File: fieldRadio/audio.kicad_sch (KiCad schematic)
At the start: 41 parts, among them J10 Conn_01x03, U6 LM386

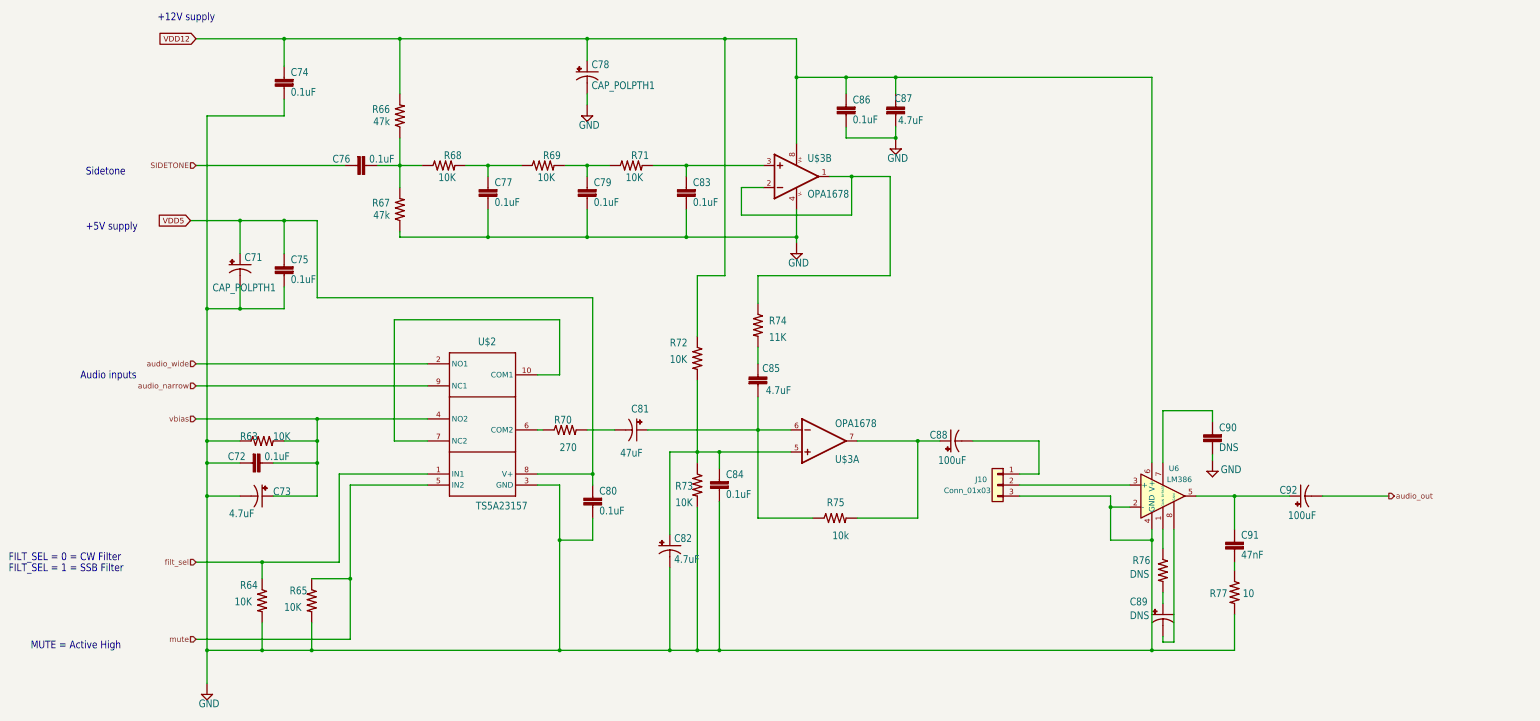
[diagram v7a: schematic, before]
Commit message: Refine Placement 2
Finish refining block placement; ready for initial routing work.
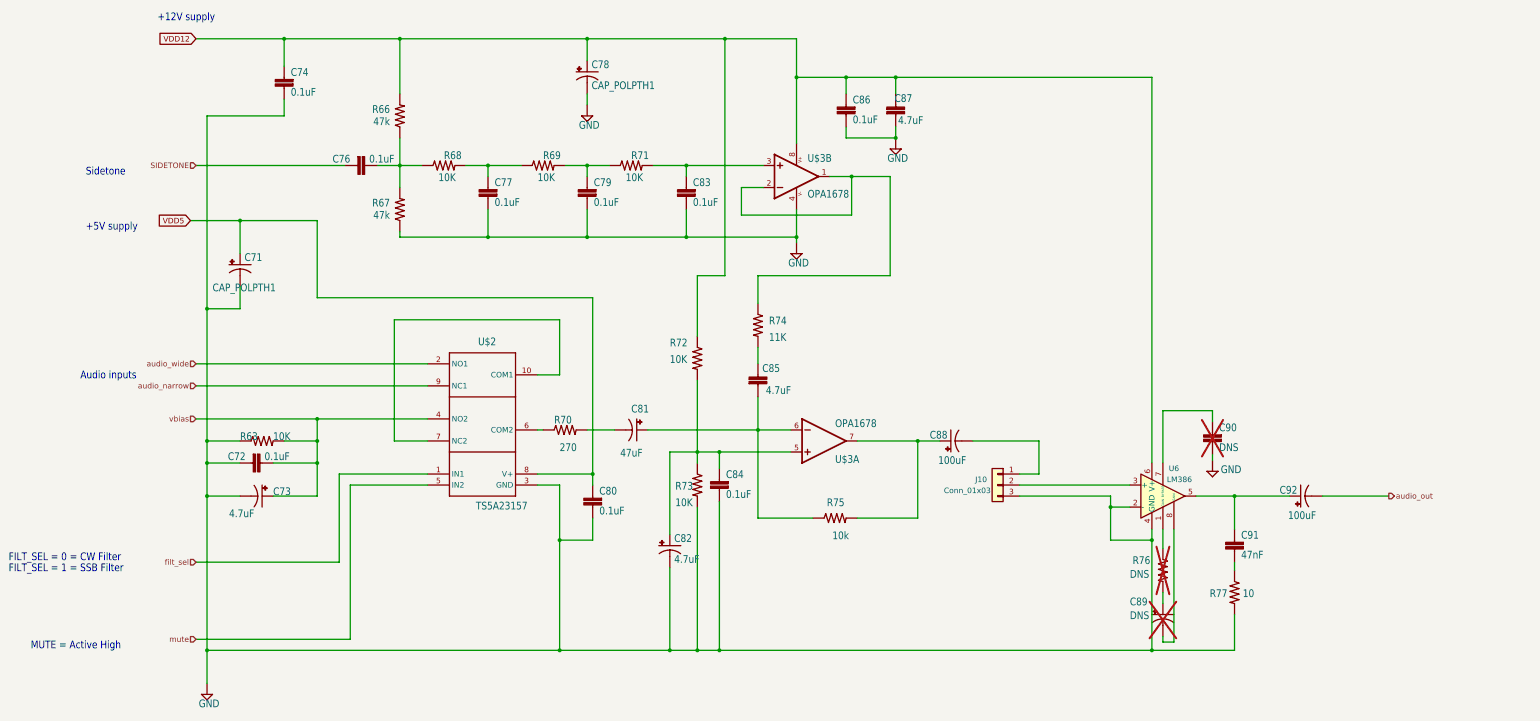
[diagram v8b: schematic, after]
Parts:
- removed C75: 0.1uF, Capacitor_SMD:C_0603_1608Metric_Pad1.08x0.95mm_HandSolder, symbol audioModule2-eagle-import:CAP0603-CAP
- removed R64, R65: 10K, Resistor_SMD:R_0603_1608Metric_Pad0.98x0.95mm_HandSolder, symbol audioModule2-eagle-import:RESISTOR0603-RES
- C89, C90, R76: now not fitted
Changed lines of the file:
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@@
   (junction (at 172.72 137.16) (diameter 0) (color 0 0 0 0)
   )
-  (junction (at 101.6 78.74) (diameter 0) (color 0 0 0 0)
-  )
   (junction (at 231.14 45.72) (diameter 0) (color 0 0 0 0)
   )
   (junction (at 109.22 124.46) (diameter 0) (color 0 0 0 0)
   )
-  (junction (at 116.84 161.29) (diameter 0) (color 0 0 0 0)
-  )
   (junction (at 196.85 177.8) (diameter 0) (color 0 0 0 0)
   )
@@
   (junction (at 109.22 129.54) (diameter 0) (color 0 0 0 0)
   )
-  (junction (at 91.44 99.06) (diameter 0) (color 0 0 0 0)
-  )
   (junction (at 194.31 66.04) (diameter 0) (color 0 0 0 0)
   )
   (junction (at 165.1 152.4) (diameter 0) (color 0 0 0 0)
   )
-  (junction (at 107.95 177.8) (diameter 0) (color 0 0 0 0)
-  )
   (junction (at 101.6 36.83) (diameter 0) (color 0 0 0 0)
   )
@@
   (junction (at 196.85 132.08) (diameter 0) (color 0 0 0 0)
   )
-  (junction (at 96.52 157.48) (diameter 0) (color 0 0 0 0)
-  )
   (junction (at 148.59 82.55) (diameter 0) (color 0 0 0 0)
   )
   (junction (at 201.93 177.8) (diameter 0) (color 0 0 0 0)
   )
-  (junction (at 96.52 177.8) (diameter 0) (color 0 0 0 0)
-  )
   (junction (at 128.27 36.83) (diameter 0) (color 0 0 0 0)
   )
   (junction (at 83.82 99.06) (diameter 0) (color 0 0 0 0)
   )
-  (wire (pts (xy 101.6 93.98) (xy 101.6 99.06))
-    (stroke (width 0) (type default))
-  )
   (wire (pts (xy 275.59 129.54) (xy 275.59 137.16))
     (stroke (width 0) (type default))
@@
     (stroke (width 0) (type default))
   )
-  (wire (pts (xy 81.28 157.48) (xy 96.52 157.48))
+  (wire (pts (xy 81.28 157.48) (xy 114.3 157.48))
     (stroke (width 0) (type default))
   )
@@
     (stroke (width 0) (type default))
   )
-  (wire (pts (xy 96.52 171.45) (xy 96.52 177.8))
-    (stroke (width 0) (type default))
-  )
-  (wire (pts (xy 116.84 161.29) (xy 116.84 139.7))
+  (wire (pts (xy 116.84 139.7) (xy 116.84 175.26))
     (stroke (width 0) (type default))
   )
@@
     (stroke (width 0) (type default))
   )
-  (wire (pts (xy 101.6 99.06) (xy 91.44 99.06))
-    (stroke (width 0) (type default))
-  )
   (wire (pts (xy 231.14 57.15) (xy 231.14 59.69))
     (stroke (width 0) (type default))
@@
     (stroke (width 0) (type default))
   )
-  (wire (pts (xy 101.6 78.74) (xy 109.22 78.74))
-    (stroke (width 0) (type default))
-  )
   (wire (pts (xy 301.625 152.4) (xy 301.625 177.8))
     (stroke (width 0) (type default))
@@
     (stroke (width 0) (type default))
   )
-  (wire (pts (xy 91.44 78.74) (xy 101.6 78.74))
+  (wire (pts (xy 91.44 78.74) (xy 109.22 78.74))
     (stroke (width 0) (type default))
   )
@@
     (stroke (width 0) (type default))
   )
-  (wire (pts (xy 96.52 157.48) (xy 96.52 161.29))
-    (stroke (width 0) (type default))
-  )
   (wire (pts (xy 128.27 59.69) (xy 128.27 66.04))
     (stroke (width 0) (type default))
@@
     (stroke (width 0) (type default))
   )
-  (wire (pts (xy 116.84 175.26) (xy 116.84 161.29))
-    (stroke (width 0) (type default))
-  )
   (wire (pts (xy 304.165 174.625) (xy 304.165 175.895))
     (stroke (width 0) (type default))
   )
-  (wire (pts (xy 101.6 86.36) (xy 101.6 78.74))
-    (stroke (width 0) (type default))
-  )
   (wire (pts (xy 160.02 114.3) (xy 165.1 114.3))
     (stroke (width 0) (type default))
@@
     (stroke (width 0) (type default))
   )
-  (wire (pts (xy 107.95 171.45) (xy 107.95 177.8))
-    (stroke (width 0) (type default))
-  )
   (wire (pts (xy 99.06 134.62) (xy 109.22 134.62))
     (stroke (width 0) (type default))
@@
     (stroke (width 0) (type default))
   )
-  (wire (pts (xy 107.95 161.29) (xy 116.84 161.29))
-    (stroke (width 0) (type default))
-  )
-  (wire (pts (xy 107.95 177.8) (xy 96.52 177.8))
-    (stroke (width 0) (type default))
-  )
   (wire (pts (xy 306.705 175.895) (xy 306.705 149.86))
     (stroke (width 0) (type default))
@@
     (stroke (width 0) (type default))
   )
-  (wire (pts (xy 107.95 177.8) (xy 165.1 177.8))
+  (wire (pts (xy 83.82 177.8) (xy 165.1 177.8))
     (stroke (width 0) (type default))
   )
@@
     (stroke (width 0) (type default))
   )
-  (wire (pts (xy 96.52 177.8) (xy 83.82 177.8))
-    (stroke (width 0) (type default))
-  )
   (wire (pts (xy 171.45 66.04) (xy 176.53 66.04))
     (stroke (width 0) (type default))
@@
   )
   (wire (pts (xy 271.145 139.7) (xy 296.545 139.7))
-    (stroke (width 0) (type default))
-  )
-  (wire (pts (xy 96.52 157.48) (xy 114.3 157.48))
     (stroke (width 0) (type default))
   )
@@
     (effects (font (size 1.27 1.27)) (justify right))
   )
-  (symbol (lib_id "audioModule2-eagle-import:CAP0603-CAP") (at 101.6 88.9 180) (unit 1)
-    (in_bom yes) (on_board yes) (dnp no)
-    (property "Reference" "C75" (at 103.124 88.773 0)
-      (effects (font (size 1.778 1.5113)) (justify right top))
-    )
-    (property "Value" "0.1uF" (at 103.124 93.345 0)
-      (effects (font (size 1.778 1.5113)) (justify right top))
-    )
-    (property "Footprint" "Capacitor_SMD:C_0603_1608Metric_Pad1.08x0.95mm_HandSolder" (at 101.6 88.9 0)
-      (effects (font (size 1.27 1.27)) hide)
-    )
-    (property "Datasheet" "" (at 101.6 88.9 0)
-      (effects (font (size 1.27 1.27)) hide)
-    )
-    (pin "1")
-    (pin "2")
-    (instances
-      (project "fieldRadio"
-        (path "/a1d1b2b0-2f27-4dc0-94ba-bb0e02933617/ac2f1cb1-df94-4091-865f-0947d1b52aed"
-          (reference "C75") (unit 1)
-        )
-      )
-      (project ""
-        (path "/c58960d9-4cac-4036-ad2e-1aef26946dae"
-          (reference "C5") (unit 1)
-        )
-      )
-    )
-  )
   (symbol (lib_id "audioModule2-eagle-import:CAP_POLPTH1") (at 171.45 44.45 0) (unit 1)
     (in_bom yes) (on_board yes) (dnp no)
@@
         (path "/c58960d9-4cac-4036-ad2e-1aef26946dae"
           (reference "#SUPPLY03") (unit 1)
-        )
-      )
-    )
-  )
-  (symbol (lib_id "audioModule2-eagle-import:RESISTOR0603-RES") (at 107.95 166.37 270) (unit 1)
-    (in_bom yes) (on_board yes) (dnp no)
-    (property "Reference" "R65" (at 102.87 165.1 90)
-      (effects (font (size 1.778 1.5113)) (justify left bottom))
-    )
-    (property "Value" "10K" (at 101.6 168.91 90)
-      (effects (font (size 1.778 1.5113)) (justify left bottom))
-    )
-    (property "Footprint" "Resistor_SMD:R_0603_1608Metric_Pad0.98x0.95mm_HandSolder" (at 107.95 166.37 0)
-      (effects (font (size 1.27 1.27)) hide)
-    )
-    (property "Datasheet" "" (at 107.95 166.37 0)
-      (effects (font (size 1.27 1.27)) hide)
-    )
-    (pin "1")
-    (pin "2")
-    (instances
-      (project "fieldRadio"
-        (path "/a1d1b2b0-2f27-4dc0-94ba-bb0e02933617/ac2f1cb1-df94-4091-865f-0947d1b52aed"
-          (reference "R65") (unit 1)
-        )
-      )
-      (project ""
-        (path "/c58960d9-4cac-4036-ad2e-1aef26946dae"
-          (reference "R3") (unit 1)
-        )
-      )
-    )
-  )
-  (symbol (lib_id "audioModule2-eagle-import:RESISTOR0603-RES") (at 96.52 166.37 270) (unit 1)
-    (in_bom yes) (on_board yes) (dnp no)
-    (property "Reference" "R64" (at 91.44 163.83 90)
-      (effects (font (size 1.778 1.5113)) (justify left bottom))
-    )
-    (property "Value" "10K" (at 90.17 167.64 90)
-      (effects (font (size 1.778 1.5113)) (justify left bottom))
-    )
-    (property "Footprint" "Resistor_SMD:R_0603_1608Metric_Pad0.98x0.95mm_HandSolder" (at 96.52 166.37 0)
-      (effects (font (size 1.27 1.27)) hide)
-    )
-    (property "Datasheet" "" (at 96.52 166.37 0)
-      (effects (font (size 1.27 1.27)) hide)
-    )
-    (pin "1")
-    (pin "2")
-    (instances
-      (project "fieldRadio"
-        (path "/a1d1b2b0-2f27-4dc0-94ba-bb0e02933617/ac2f1cb1-df94-4091-865f-0947d1b52aed"
-          (reference "R64") (unit 1)
-        )
-      )
-      (project ""
-        (path "/c58960d9-4cac-4036-ad2e-1aef26946dae"
-          (reference "R2") (unit 1)
         )
       )
@@
   )
   (symbol (lib_id "audioModule2-eagle-import:RESISTOR0603-RES") (at 304.165 159.385 270) (unit 1)
-    (in_bom yes) (on_board yes) (dnp no)
+    (in_bom yes) (on_board yes) (dnp yes)
     (property "Reference" "R76" (at 297.18 158.115 90)
       (effects (font (size 1.778 1.5113)) (justify left bottom))
@@
     )
     (property "Datasheet" "" (at 304.165 159.385 0)
+      (effects (font (size 1.27 1.27)) hide)
+    )
+    (property "Mouser Part Number" "" (at 304.165 159.385 0)
       (effects (font (size 1.27 1.27)) hide)
     )
@@
   )
   (symbol (lib_id "audioModule2-eagle-import:CAP_POLPTH1") (at 304.165 169.545 0) (unit 1)
-    (in_bom yes) (on_board yes) (dnp no)
+    (in_bom yes) (on_board yes) (dnp yes)
     (property "Reference" "C89" (at 296.545 167.64 0)
       (effects (font (size 1.778 1.5113)) (justify left bottom))
@@
     )
     (property "Datasheet" "" (at 304.165 169.545 0)
+      (effects (font (size 1.27 1.27)) hide)
+    )
+    (property "Mouser Part Number" "" (at 304.165 169.545 0)
       (effects (font (size 1.27 1.27)) hide)
     )
@@
   )
   (symbol (lib_id "audioModule2-eagle-import:CAP0603-CAP") (at 315.595 127.635 180) (unit 1)
-    (in_bom yes) (on_board yes) (dnp no)
+    (in_bom yes) (on_board yes) (dnp yes)
     (property "Reference" "C90" (at 317.119 127.508 0)
       (effects (font (size 1.778 1.5113)) (justify right top))
@@
       (effects (font (size 1.27 1.27)) hide)
     )
+    (property "Mouser Part Number" "" (at 315.595 127.635 0)
+      (effects (font (size 1.27 1.27)) hide)
+    )
